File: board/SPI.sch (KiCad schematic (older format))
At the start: 38 parts, among them P14 CONN_5X2, P3 CONN_7X2, U11 MICRO_SD, U17 FXO-HC536R, U26 CB3LV-3I-27M0000, U3 W25Q128FVEIG

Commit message: Importing footprint names into schematic.
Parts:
- C132: footprint (none) -> SM0402
- C188, C189, C241, C244, C36, R116, R117, R118, R119, R16, R17, R18, R19, R20, R21, R40, R41, R60, R61, R62, R63, R64, R76, R80, R81, R82, R83, R86, R93: footprint (none) -> SM0603
- JP1, JP2: footprint (none) -> GS2
- P14: footprint (none) -> PIN_ARRAY_5x2
- P3: footprint (none) -> JTAG
- U11: footprint ~ -> MicroSD
- U17: footprint ~ -> FXO-HC536R
- U26: footprint ~ -> CB3LV-3I
- U3: footprint ~ -> SO8E_N
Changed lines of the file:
@@
 Sheet 4 12
 Title "HDMI2USB"
-Date "5 jul 2015"
+Date "23 jul 2015"
 Rev "Rev2"
 Comp ""
@@
 F 0 "U3" H 3850 6250 60  0000 C CNN
 F 1 "W25Q128FVEIG" H 3850 5400 60  0000 C CNN
-F 2 "~" H 3850 5800 60  0000 C CNN
+F 2 "SO8E_N" H 3850 5800 60  0001 C CNN
 F 3 "~" H 3850 5800 60  0000 C CNN
 F 4 "Yes" H 3850 5800 60  0001 C CNN "Populate"
@@
 F 0 "R16" V 2430 5700 50  0000 C CNN
 F 1 "50R" V 2350 5700 50  0000 C CNN
-F 2 "" H 2350 5700 60  0000 C CNN
+F 2 "SM0603" H 2350 5700 60  0001 C CNN
 F 3 "" H 2350 5700 60  0000 C CNN
 F 4 "Yes" H 2350 5700 60  0001 C CNN "Populate"
@@
 F 0 "R17" V 2430 5850 50  0000 C CNN
 F 1 "50R" V 2350 5850 50  0000 C CNN
-F 2 "" H 2350 5850 60  0000 C CNN
+F 2 "SM0603" H 2350 5850 60  0001 C CNN
 F 3 "" H 2350 5850 60  0000 C CNN
 F 4 "Yes" H 2350 5850 60  0001 C CNN "Populate"
@@
 F 0 "R20" V 3280 5250 50  0000 C CNN
 F 1 "10K" V 3200 5250 50  0000 C CNN
-F 2 "" H 3200 5250 60  0000 C CNN
+F 2 "SM0603" H 3200 5250 60  0001 C CNN
 F 3 "" H 3200 5250 60  0000 C CNN
 F 4 "Yes" H 3200 5250 60  0001 C CNN "Populate"
@@
 F 0 "R19" V 3280 5050 50  0000 C CNN
 F 1 "10K" V 3200 5050 50  0000 C CNN
-F 2 "" H 3200 5050 60  0000 C CNN
+F 2 "SM0603" H 3200 5050 60  0001 C CNN
 F 3 "" H 3200 5050 60  0000 C CNN
 F 4 "Yes" H 3200 5050 60  0001 C CNN "Populate"
@@
 F 0 "R18" V 3280 4850 50  0000 C CNN
 F 1 "10K" V 3200 4850 50  0000 C CNN
-F 2 "" H 3200 4850 60  0000 C CNN
+F 2 "SM0603" H 3200 4850 60  0001 C CNN
 F 3 "" H 3200 4850 60  0000 C CNN
 F 4 "Yes" H 3200 4850 60  0001 C CNN "Populate"
@@
 F 0 "R21" V 5330 5250 50  0000 C CNN
 F 1 "10K" V 5250 5250 50  0000 C CNN
-F 2 "" H 5250 5250 60  0000 C CNN
+F 2 "SM0603" H 5250 5250 60  0001 C CNN
 F 3 "" H 5250 5250 60  0000 C CNN
 F 4 "Yes" H 5250 5250 60  0001 C CNN "Populate"
@@
 F 0 "C36" H 4600 5000 50  0000 L CNN
 F 1 "0.1UF" V 4600 4600 50  0000 L CNN
-F 2 "" H 4550 4900 60  0000 C CNN
+F 2 "SM0603" H 4550 4900 60  0001 C CNN
 F 3 "" H 4550 4900 60  0000 C CNN
 F 4 "Yes" H 4550 4900 60  0001 C CNN "Populate"
@@
 F 0 "JP1" H 5750 1850 60  0000 C CNN
 F 1 "JUMPER" H 5750 1620 40  0000 C CNN
-F 2 "" H 5750 1700 60  0000 C CNN
+F 2 "GS2" H 5750 1700 60  0001 C CNN
 F 3 "" H 5750 1700 60  0000 C CNN
 F 4 "Yes" H 5750 1700 60  0001 C CNN "Populate"
@@
 F 0 "JP2" H 5750 2200 60  0000 C CNN
 F 1 "JUMPER" H 5750 1970 40  0000 C CNN
-F 2 "" H 5750 2050 60  0000 C CNN
+F 2 "GS2" H 5750 2050 60  0001 C CNN
 F 3 "" H 5750 2050 60  0000 C CNN
 F 4 "Yes" H 5750 2050 60  0001 C CNN "Populate"
@@
 F 0 "R60" V 8700 1400 50  0000 C CNN
 F 1 "100K" V 8650 1200 50  0000 C CNN
-F 2 "" H 8650 1200 60  0000 C CNN
+F 2 "SM0603" H 8650 1200 60  0001 C CNN
 F 3 "" H 8650 1200 60  0000 C CNN
 F 4 "Yes" H 8650 1200 60  0001 C CNN "Populate"
@@
 F 0 "R61" V 8700 1550 50  0000 C CNN
 F 1 "100K" V 8650 1350 50  0000 C CNN
-F 2 "" H 8650 1350 60  0000 C CNN
+F 2 "SM0603" H 8650 1350 60  0001 C CNN
 F 3 "" H 8650 1350 60  0000 C CNN
 F 4 "Yes" H 8650 1350 60  0001 C CNN "Populate"
@@
 F 0 "R62" V 8700 1700 50  0000 C CNN
 F 1 "100K" V 8650 1500 50  0000 C CNN
-F 2 "" H 8650 1500 60  0000 C CNN
+F 2 "SM0603" H 8650 1500 60  0001 C CNN
 F 3 "" H 8650 1500 60  0000 C CNN
 F 4 "Yes" H 8650 1500 60  0001 C CNN "Populate"
@@
 F 0 "R63" V 8700 1850 50  0000 C CNN
 F 1 "100K" V 8650 1650 50  0000 C CNN
-F 2 "" H 8650 1650 60  0000 C CNN
+F 2 "SM0603" H 8650 1650 60  0001 C CNN
 F 3 "" H 8650 1650 60  0000 C CNN
 F 4 "Yes" H 8650 1650 60  0001 C CNN "Populate"
@@
 F 0 "R64" V 8750 1700 50  0000 C CNN
 F 1 "100K" V 8650 1800 50  0000 C CNN
-F 2 "" H 8650 1800 60  0000 C CNN
+F 2 "SM0603" H 8650 1800 60  0001 C CNN
 F 3 "" H 8650 1800 60  0000 C CNN
 F 4 "Yes" H 8650 1800 60  0001 C CNN "Populate"
@@
 F 0 "C132" H 8100 1550 50  0000 L CNN
 F 1 "0.1UF" V 7900 1400 50  0000 L CNN
-F 2 "" H 8050 1450 60  0000 C CNN
+F 2 "SM0402" H 8050 1450 60  0001 C CNN
 F 3 "" H 8050 1450 60  0000 C CNN
 F 4 "Yes" H 8050 1450 60  0001 C CNN "Populate"
@@
 F 0 "U17" H 1650 2850 60  0000 C CNN
 F 1 "FXO-HC536R" H 1800 3400 60  0000 C CNN
-F 2 "~" H 1800 3150 60  0000 C CNN
+F 2 "FXO-HC536R" H 1800 3150 60  0001 C CNN
 F 3 "~" H 1800 3150 60  0000 C CNN
 F 4 "Yes" H 1800 3150 60  0001 C CNN "Populate"
@@
 F 0 "R80" V 1550 2900 50  0000 C CNN
 F 1 "4K7" V 1500 2700 50  0000 C CNN
-F 2 "" H 1500 2700 60  0000 C CNN
+F 2 "SM0603" H 1500 2700 60  0001 C CNN
 F 3 "" H 1500 2700 60  0000 C CNN
 F 4 "Yes" H 1500 2700 60  0001 C CNN "Populate"
@@
 F 0 "C188" H 950 3050 50  0000 L CNN
 F 1 "0.1UF" V 750 2900 50  0000 L CNN
-F 2 "" H 900 2950 60  0000 C CNN
+F 2 "SM0603" H 900 2950 60  0001 C CNN
 F 3 "" H 900 2950 60  0000 C CNN
 F 4 "Yes" H 900 2950 60  0001 C CNN "Populate"
@@
 F 0 "C189" H 2450 3650 50  0000 L CNN
 F 1 "15PF" V 2250 3500 50  0000 L CNN
-F 2 "" H 2400 3550 60  0000 C CNN
+F 2 "SM0603" H 2400 3550 60  0001 C CNN
 F 3 "" H 2400 3550 60  0000 C CNN
 F 4 "Yes" H 2400 3550 60  0001 C CNN "Populate"
@@
 F 0 "U11" H 9550 2500 60  0000 C CNN
 F 1 "MICRO_SD" H 9450 2800 60  0000 C CNN
-F 2 "~" H 9550 2350 60  0000 C CNN
+F 2 "MicroSD" H 9550 2350 60  0001 C CNN
 F 3 "~" H 9550 2350 60  0000 C CNN
 F 4 "Yes" H 9550 2350 60  0001 C CNN "Populate"
@@
 F 0 "P3" H 9850 4050 60  0000 C CNN
 F 1 "CONN_7X2" V 9850 4050 60  0001 C CNN
-F 2 "" H 9850 4050 60  0000 C CNN
+F 2 "JTAG" H 9850 4050 60  0001 C CNN
 F 3 "" H 9850 4050 60  0000 C CNN
 F 4 "Yes" H 9850 4050 60  0001 C CNN "Populate"
@@
 F 0 "R40" V 5530 1450 50  0000 C CNN
 F 1 "10K" V 5450 1450 50  0000 C CNN
-F 2 "" H 5450 1450 60  0000 C CNN
+F 2 "SM0603" H 5450 1450 60  0001 C CNN
 F 3 "" H 5450 1450 60  0000 C CNN
 F 4 "Yes" H 5450 1450 60  0001 C CNN "Populate"
@@
 F 0 "R41" V 5530 2300 50  0000 C CNN
 F 1 "10K" V 5450 2300 50  0000 C CNN
-F 2 "" H 5450 2300 60  0000 C CNN
+F 2 "SM0603" H 5450 2300 60  0001 C CNN
 F 3 "" H 5450 2300 60  0000 C CNN
 F 4 "Yes" H 5450 2300 60  0001 C CNN "Populate"
@@
 F 0 "R76" V 9150 3650 50  0000 C CNN
 F 1 "100R" V 9200 3850 50  0000 C CNN
-F 2 "" H 9200 3850 60  0000 C CNN
+F 2 "SM0603" H 9200 3850 60  0001 C CNN
 F 3 "" H 9200 3850 60  0000 C CNN
 F 4 "Yes" H 9200 3850 60  0001 C CNN "Populate"
@@
 F 0 "R81" V 9150 3750 50  0000 C CNN
 F 1 "100R" V 9200 3950 50  0000 C CNN
-F 2 "" H 9200 3950 60  0000 C CNN
+F 2 "SM0603" H 9200 3950 60  0001 C CNN
 F 3 "" H 9200 3950 60  0000 C CNN
 F 4 "Yes" H 9200 3950 60  0001 C CNN "Populate"
@@
 F 0 "R82" V 9150 3850 50  0000 C CNN
 F 1 "100R" V 9200 4050 50  0000 C CNN
-F 2 "" H 9200 4050 60  0000 C CNN
+F 2 "SM0603" H 9200 4050 60  0001 C CNN
 F 3 "" H 9200 4050 60  0000 C CNN
 F 4 "Yes" H 9200 4050 60  0001 C CNN "Populate"
@@
 F 0 "R83" V 9150 3950 50  0000 C CNN
 F 1 "100R" V 9200 4150 50  0000 C CNN
-F 2 "" H 9200 4150 60  0000 C CNN
+F 2 "SM0603" H 9200 4150 60  0001 C CNN
 F 3 "" H 9200 4150 60  0000 C CNN
 F 4 "Yes" H 9200 4150 60  0001 C CNN "Populate"
@@
 F 0 "U26" H 1600 1100 60  0000 C CNN
 F 1 "CB3LV-3I-27M0000" H 1750 1650 60  0000 C CNN
-F 2 "~" H 1750 1400 60  0000 C CNN
+F 2 "CB3LV-3I" H 1750 1400 60  0001 C CNN
 F 3 "~" H 1750 1400 60  0000 C CNN
 F 4 "Yes" H 1750 1400 60  0001 C CNN "Populate"
@@
 F 0 "R86" V 1500 1150 50  0000 C CNN
 F 1 "4K7" V 1450 950 50  0000 C CNN
-F 2 "" H 1450 950 60  0000 C CNN
+F 2 "SM0603" H 1450 950 60  0001 C CNN
 F 3 "" H 1450 950 60  0000 C CNN
 F 4 "Yes" H 1450 950 60  0001 C CNN "Populate"
@@
 F 0 "C241" H 900 1300 50  0000 L CNN
 F 1 "0.1UF" V 700 1150 50  0000 L CNN
-F 2 "" H 850 1200 60  0000 C CNN
+F 2 "SM0603" H 850 1200 60  0001 C CNN
 F 3 "" H 850 1200 60  0000 C CNN
 F 4 "Yes" H 850 1200 60  0001 C CNN "Populate"
@@
 F 0 "C244" H 2400 1900 50  0000 L CNN
 F 1 "15PF" V 2200 1750 50  0000 L CNN
-F 2 "" H 2350 1800 60  0000 C CNN
+F 2 "SM0603" H 2350 1800 60  0001 C CNN
 F 3 "" H 2350 1800 60  0000 C CNN
 F 4 "Yes" H 2350 1800 60  0001 C CNN "Populate"
@@
 F 0 "P14" H 9200 6100 60  0000 C CNN
 F 1 "CONN_5X2" V 9200 5800 50  0001 C CNN
-F 2 "" H 9200 5800 60  0000 C CNN
+F 2 "PIN_ARRAY_5x2" H 9200 5800 60  0001 C CNN
 F 3 "" H 9200 5800 60  0000 C CNN
 F 4 "Yes" H 9200 5800 60  0001 C CNN "Populate"
@@
 F 0 "R93" V 7930 5350 50  0000 C CNN
 F 1 "100R" V 7850 5350 50  0000 C CNN
-F 2 "" H 7850 5350 60  0000 C CNN
+F 2 "SM0603" H 7850 5350 60  0001 C CNN
 F 3 "" H 7850 5350 60  0000 C CNN
 F 4 "Yes" H 7850 5350 60  0001 C CNN "Populate"
@@
 F 0 "R118" V 10030 5600 50  0000 C CNN
 F 1 "100R" V 9950 5600 50  0000 C CNN
-F 2 "" H 9950 5600 60  0000 C CNN
+F 2 "SM0603" H 9950 5600 60  0001 C CNN
 F 3 "" H 9950 5600 60  0000 C CNN
 F 4 "Yes" H 9950 5600 60  0001 C CNN "Populate"
@@
 F 0 "R116" V 8180 5800 50  0000 C CNN
 F 1 "100R" V 8100 5800 50  0000 C CNN
-F 2 "" H 8100 5800 60  0000 C CNN
+F 2 "SM0603" H 8100 5800 60  0001 C CNN
 F 3 "" H 8100 5800 60  0000 C CNN
 F 4 "Yes" H 8100 5800 60  0001 C CNN "Populate"
@@
 F 0 "R117" V 9730 5300 50  0000 C CNN
 F 1 "1M" V 9650 5300 50  0000 C CNN
-F 2 "" H 9650 5300 60  0000 C CNN
+F 2 "SM0603" H 9650 5300 60  0001 C CNN
 F 3 "" H 9650 5300 60  0000 C CNN
 F 4 "Yes" H 9650 5300 60  0001 C CNN "Populate"
@@
 F 0 "R119" V 10000 5650 50  0000 C CNN
 F 1 "1K" V 9950 5900 50  0000 C CNN
-F 2 "" H 9950 5900 60  0000 C CNN
+F 2 "SM0603" H 9950 5900 60  0001 C CNN
 F 3 "" H 9950 5900 60  0000 C CNN
 F 4 "Yes" H 9950 5900 60  0001 C CNN "Populate"

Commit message: Changes on 2015-10-21@7-21PM
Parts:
- added P28: CONN_6, symbol CONN_6
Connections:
- net SD_CLK: now also P28.3
- net SD_CMD: now also P28.4
- net SD_DAT0: now also P28.2
- net SD_DAT1: now also P28.1
- net SD_DAT2: now also P28.6
- net SD_DAT3: now also P28.5
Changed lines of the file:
@@
 Sheet 4 12
 Title "HDMI2USB"
-Date "10 sep 2015"
+Date "19 oct 2015"
 Rev "Rev2"
 Comp ""
@@
 $EndComp
 $Comp
-L GND #PWR023
+L GND #PWR26
 U 1 1 52D67B63
 P 2750 6100
-F 0 "#PWR023" H 2750 6100 30  0001 C CNN
+F 0 "#PWR26" H 2750 6100 30  0001 C CNN
 F 1 "GND" H 2750 6030 30  0001 C CNN
 F 2 "" H 2750 6100 60  0000 C CNN
@@
 $EndComp
 $Comp
-L GND #PWR024
+L GND #PWR27
 U 1 1 52D67F2B
 P 4350 5050
-F 0 "#PWR024" H 4350 5050 30  0001 C CNN
+F 0 "#PWR27" H 4350 5050 30  0001 C CNN
 F 1 "GND" H 4350 4980 30  0001 C CNN
 F 2 "" H 4350 5050 60  0000 C CNN
@@
 FPGA_M1
 $Comp
-L GND #PWR025
+L GND #PWR31
 U 1 1 52E410EA
 P 9850 2850
-F 0 "#PWR025" H 9850 2850 30  0001 C CNN
+F 0 "#PWR31" H 9850 2850 30  0001 C CNN
 F 1 "GND" H 9850 2780 30  0001 C CNN
 F 2 "" H 9850 2850 60  0000 C CNN
@@
 $EndComp
 $Comp
-L GND #PWR026
+L GND #PWR30
 U 1 1 52E4224F
 P 8050 1700
-F 0 "#PWR026" H 8050 1700 30  0001 C CNN
+F 0 "#PWR30" H 8050 1700 30  0001 C CNN
 F 1 "GND" H 8050 1630 30  0001 C CNN
 F 2 "" H 8050 1700 60  0000 C CNN
@@
 	1    0    0    -1
 $EndComp
-Text HLabel 8000 2600 0    60   BiDi ~ 12
+Text HLabel 7950 2550 2    60   BiDi ~ 12
 SD_DAT0
-Text HLabel 8000 2700 0    60   BiDi ~ 12
+Text HLabel 7500 2650 2    60   BiDi ~ 12
 SD_DAT1
-Text HLabel 8000 2400 0    60   Input ~ 12
+Text HLabel 8000 2350 2    60   Input ~ 12
 SD_CLK
-Text HLabel 8000 2200 0    60   BiDi ~ 12
+Text HLabel 7400 2200 2    60   BiDi ~ 12
 SD_CMD
-Text HLabel 8000 2100 0    60   BiDi ~ 12
+Text HLabel 7400 2100 2    60   BiDi ~ 12
 SD_DAT3
-Text HLabel 8000 2000 0    60   BiDi ~ 12
+Text HLabel 7400 2000 2    60   BiDi ~ 12
 SD_DAT2
 Text Label 7800 1200 0    60   ~ 0
@@
 JTAG\n
 $Comp
-L GND #PWR027
+L GND #PWR32
 U 1 1 52E36A0E
 P 10350 4450
-F 0 "#PWR027" H 10350 4450 30  0001 C CNN
+F 0 "#PWR32" H 10350 4450 30  0001 C CNN
 F 1 "GND" H 10350 4380 30  0001 C CNN
 F 2 "" H 10350 4450 60  0000 C CNN
@@
 $EndComp
 $Comp
-L GND #PWR028
+L GND #PWR23
 U 1 1 52E638C7
 P 900 3400
-F 0 "#PWR028" H 900 3400 30  0001 C CNN
+F 0 "#PWR23" H 900 3400 30  0001 C CNN
 F 1 "GND" H 900 3330 30  0001 C CNN
 F 2 "" H 900 3400 60  0000 C CNN
@@
 $EndComp
 $Comp
-L GND #PWR029
+L GND #PWR25
 U 1 1 530C0275
 P 2400 3850
-F 0 "#PWR029" H 2400 3850 30  0001 C CNN
+F 0 "#PWR25" H 2400 3850 30  0001 C CNN
 F 1 "GND" H 2400 3780 30  0001 C CNN
 F 2 "" H 2400 3850 60  0000 C CNN
@@
 VCC3V3
 $Comp
-L GND #PWR030
+L GND #PWR28
 U 1 1 5392B9BD
 P 6650 2000
-F 0 "#PWR030" H 6650 2000 30  0001 C CNN
+F 0 "#PWR28" H 6650 2000 30  0001 C CNN
 F 1 "GND" H 6650 1930 30  0001 C CNN
 F 2 "" H 6650 2000 60  0000 C CNN
@@
 Connection ~ 9850 2800
 Wire Wire Line
-	8000 2600 9250 2600
-Wire Wire Line
-	8000 2700 9250 2700
+	7950 2600 9250 2600
+Wire Wire Line
+	7500 2700 9250 2700
 Wire Wire Line
 	8000 2400 9250 2400
@@
 	8950 1650 8950 2600
 Wire Wire Line
-	8000 2200 9250 2200
+	7400 2200 9250 2200
 Wire Wire Line
 	9000 2200 9000 1500
@@
 	9000 1500 8900 1500
 Wire Wire Line
-	8000 2100 9250 2100
+	7400 2100 9250 2100
 Wire Wire Line
 	9050 2100 9050 1350
@@
 	9100 1200 9100 2000
 Wire Wire Line
-	8000 2000 9250 2000
+	7400 2000 9250 2000
 Connection ~ 8950 2600
 Connection ~ 8900 2700
@@
 $EndComp
 $Comp
-L GND #PWR031
+L GND #PWR22
 U 1 1 551C2E78
 P 850 1650
-F 0 "#PWR031" H 850 1650 30  0001 C CNN
+F 0 "#PWR22" H 850 1650 30  0001 C CNN
 F 1 "GND" H 850 1580 30  0001 C CNN
 F 2 "" H 850 1650 60  0000 C CNN
@@
 $EndComp
 $Comp
-L GND #PWR032
+L GND #PWR24
 U 1 1 551C2E86
 P 2350 2100
-F 0 "#PWR032" H 2350 2100 30  0001 C CNN
+F 0 "#PWR24" H 2350 2100 30  0001 C CNN
 F 1 "GND" H 2350 2030 30  0001 C CNN
 F 2 "" H 2350 2100 60  0000 C CNN
@@
 	7850 5800 7750 5800
 $Comp
-L GND #PWR033
+L GND #PWR33
 U 1 1 551DEA2A
 P 10400 5950
-F 0 "#PWR033" H 10400 5950 30  0001 C CNN
+F 0 "#PWR33" H 10400 5950 30  0001 C CNN
 F 1 "GND" H 10400 5880 30  0001 C CNN
 F 2 "" H 10400 5950 60  0000 C CNN
@@
 NoConn ~ 8800 6000
 $Comp
-L GND #PWR034
+L GND #PWR29
 U 1 1 551DEF69
 P 7750 5900
-F 0 "#PWR034" H 7750 5900 30  0001 C CNN
+F 0 "#PWR29" H 7750 5900 30  0001 C CNN
 F 1 "GND" H 7750 5830 30  0001 C CNN
 F 2 "" H 7750 5900 60  0000 C CNN
@@
 Text Label 9650 4950 0    60   ~ 0
 VCC1V5
+$Comp
+L CONN_6 P28
+U 1 1 56254665
+P 7050 2250
+F 0 "P28" V 7000 2250 60  0000 C CNN
+F 1 "CONN_6" V 7100 2250 60  0000 C CNN
+F 2 "" H 7050 2250 60  0000 C CNN
+F 3 "" H 7050 2250 60  0000 C CNN
+	1    7050 2250
+	-1   0    0    1
+$EndComp
+Wire Wire Line
+	8000 2400 8000 2300
+Wire Wire Line
+	8000 2300 7400 2300
+Wire Wire Line
+	7400 2400 7950 2400
+Wire Wire Line
+	7500 2700 7500 2500
+Wire Wire Line
+	7500 2500 7400 2500
+Wire Wire Line
+	7950 2400 7950 2600
 $EndSCHEMATC

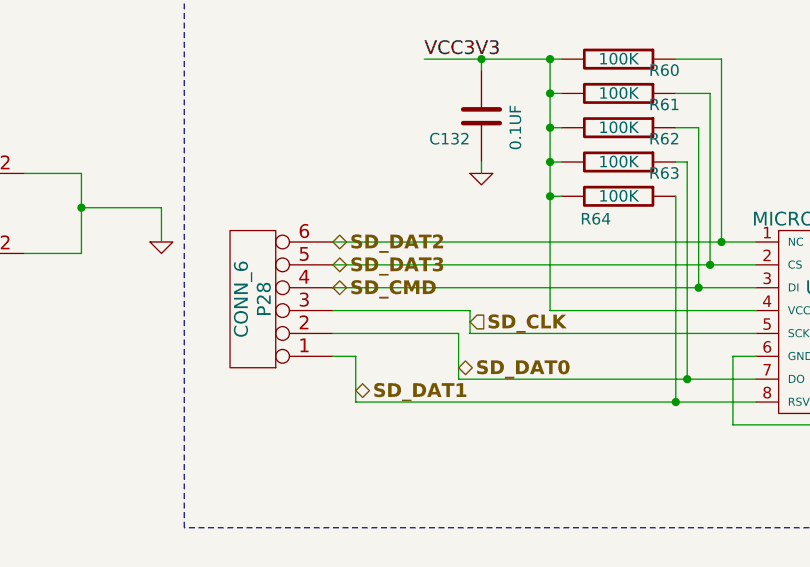
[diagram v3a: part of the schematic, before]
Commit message: Changes on 12-11-2015 Micro SD header added.#35
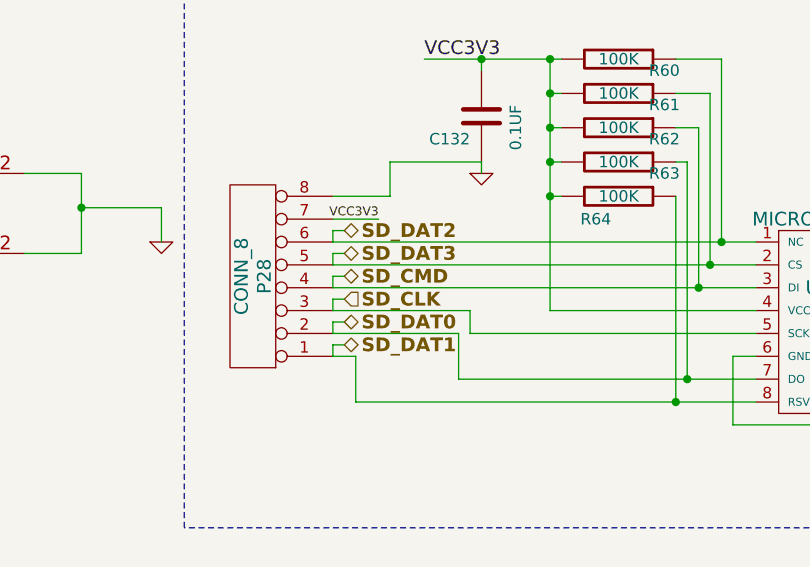
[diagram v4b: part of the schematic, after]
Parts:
- removed P28: CONN_6, symbol CONN_6
- added P28: CONN_8, symbol CONN_8
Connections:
- net GND: now also P28.8 (P8)
- net SD_CLK: now also P28.3 (P3)
- net SD_CMD: now also P28.4 (P4)
- net SD_DAT0: now also P28.2 (P2)
- net SD_DAT1: now also P28.1 (P1)
- net SD_DAT2: now also P28.6 (P6)
- net SD_DAT3: now also P28.5 (P5)
- net VCC3V3: now also P28.7 (P7)

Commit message: Final changes
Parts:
- C132, C188, C241, C36: value 0.1UF -> 0.1uF
- C189, C244: value 15PF -> 15pF
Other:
- note added: "135MHz"
- note removed: "100MHz"
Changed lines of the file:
@@
 LIBS:contrib
 LIBS:valves
-LIBS:hdmi2usb
-LIBS:timvideos-pcie-8x
 LIBS:HDMI2USB-cache
 EELAYER 27 0
@@
 Sheet 4 12
 Title "HDMI2USB"
-Date "2 nov 2015"
+Date "9 nov 2015"
 Rev "Rev2"
 Comp ""
@@
 $EndComp
 $Comp
-L GND #PWR26
+L GND #PWR023
 U 1 1 52D67B63
 P 2750 6100
-F 0 "#PWR26" H 2750 6100 30  0001 C CNN
+F 0 "#PWR023" H 2750 6100 30  0001 C CNN
 F 1 "GND" H 2750 6030 30  0001 C CNN
 F 2 "" H 2750 6100 60  0000 C CNN
@@
 P 4550 4900
 F 0 "C36" H 4600 5000 50  0000 L CNN
-F 1 "0.1UF" V 4600 4600 50  0000 L CNN
+F 1 "0.1uF" V 4600 4600 50  0000 L CNN
 F 2 "SM0603" H 4550 4900 60  0001 C CNN
 F 3 "" H 4550 4900 60  0000 C CNN
@@
 $EndComp
 $Comp
-L GND #PWR27
+L GND #PWR024
 U 1 1 52D67F2B
 P 4350 5050
-F 0 "#PWR27" H 4350 5050 30  0001 C CNN
+F 0 "#PWR024" H 4350 5050 30  0001 C CNN
 F 1 "GND" H 4350 4980 30  0001 C CNN
 F 2 "" H 4350 5050 60  0000 C CNN
@@
 FPGA_M1
 $Comp
-L GND #PWR31
+L GND #PWR025
 U 1 1 52E410EA
 P 9850 2850
-F 0 "#PWR31" H 9850 2850 30  0001 C CNN
+F 0 "#PWR025" H 9850 2850 30  0001 C CNN
 F 1 "GND" H 9850 2780 30  0001 C CNN
 F 2 "" H 9850 2850 60  0000 C CNN
@@
 P 8050 1450
 F 0 "C132" H 8100 1550 50  0000 L CNN
-F 1 "0.1UF" V 7900 1400 50  0000 L CNN
+F 1 "0.1uF" V 7900 1400 50  0000 L CNN
 F 2 "SM0402" H 8050 1450 60  0001 C CNN
 F 3 "" H 8050 1450 60  0000 C CNN
@@
 $EndComp
 $Comp
-L GND #PWR30
+L GND #PWR026
 U 1 1 52E4224F
 P 8050 1700
-F 0 "#PWR30" H 8050 1700 30  0001 C CNN
+F 0 "#PWR026" H 8050 1700 30  0001 C CNN
 F 1 "GND" H 8050 1630 30  0001 C CNN
 F 2 "" H 8050 1700 60  0000 C CNN
@@
 JTAG\n
 $Comp
-L GND #PWR32
+L GND #PWR027
 U 1 1 52E36A0E
 P 10350 4450
-F 0 "#PWR32" H 10350 4450 30  0001 C CNN
+F 0 "#PWR027" H 10350 4450 30  0001 C CNN
 F 1 "GND" H 10350 4380 30  0001 C CNN
 F 2 "" H 10350 4450 60  0000 C CNN
@@
 P 900 2950
 F 0 "C188" H 950 3050 50  0000 L CNN
-F 1 "0.1UF" V 750 2900 50  0000 L CNN
+F 1 "0.1uF" V 750 2900 50  0000 L CNN
 F 2 "SM0603" H 900 2950 60  0001 C CNN
 F 3 "" H 900 2950 60  0000 C CNN
@@
 $EndComp
 $Comp
-L GND #PWR23
+L GND #PWR028
 U 1 1 52E638C7
 P 900 3400
-F 0 "#PWR23" H 900 3400 30  0001 C CNN
+F 0 "#PWR028" H 900 3400 30  0001 C CNN
 F 1 "GND" H 900 3330 30  0001 C CNN
 F 2 "" H 900 3400 60  0000 C CNN
@@
 P 2400 3550
 F 0 "C189" H 2450 3650 50  0000 L CNN
-F 1 "15PF" V 2250 3500 50  0000 L CNN
+F 1 "15pF" V 2250 3500 50  0000 L CNN
 F 2 "SM0603" H 2400 3550 60  0001 C CNN
 F 3 "" H 2400 3550 60  0000 C CNN
@@
 $EndComp
 $Comp
-L GND #PWR25
+L GND #PWR029
 U 1 1 530C0275
 P 2400 3850
-F 0 "#PWR25" H 2400 3850 30  0001 C CNN
+F 0 "#PWR029" H 2400 3850 30  0001 C CNN
 F 1 "GND" H 2400 3780 30  0001 C CNN
 F 2 "" H 2400 3850 60  0000 C CNN
@@
 VCC3V3
 $Comp
-L GND #PWR28
+L GND #PWR030
 U 1 1 5392B9BD
 P 6650 2000
-F 0 "#PWR28" H 6650 2000 30  0001 C CNN
+F 0 "#PWR030" H 6650 2000 30  0001 C CNN
 F 1 "GND" H 6650 1930 30  0001 C CNN
 F 2 "" H 6650 2000 60  0000 C CNN
@@
 $EndComp
 Text Notes 2550 3200 0    60   ~ 0
-100MHz
+135MHz
 $Comp
 L FXO-HC536R U26
@@
 P 850 1200
 F 0 "C241" H 900 1300 50  0000 L CNN
-F 1 "0.1UF" V 700 1150 50  0000 L CNN
+F 1 "0.1uF" V 700 1150 50  0000 L CNN
 F 2 "SM0603" H 850 1200 60  0001 C CNN
 F 3 "" H 850 1200 60  0000 C CNN
@@
 $EndComp
 $Comp
-L GND #PWR22
+L GND #PWR031
 U 1 1 551C2E78
 P 850 1650
-F 0 "#PWR22" H 850 1650 30  0001 C CNN
+F 0 "#PWR031" H 850 1650 30  0001 C CNN
 F 1 "GND" H 850 1580 30  0001 C CNN
 F 2 "" H 850 1650 60  0000 C CNN
@@
 P 2350 1800
 F 0 "C244" H 2400 1900 50  0000 L CNN
-F 1 "15PF" V 2200 1750 50  0000 L CNN
+F 1 "15pF" V 2200 1750 50  0000 L CNN
 F 2 "SM0603" H 2350 1800 60  0001 C CNN
 F 3 "" H 2350 1800 60  0000 C CNN
@@
 $EndComp
 $Comp
-L GND #PWR24
+L GND #PWR032
 U 1 1 551C2E86
 P 2350 2100
-F 0 "#PWR24" H 2350 2100 30  0001 C CNN
+F 0 "#PWR032" H 2350 2100 30  0001 C CNN
 F 1 "GND" H 2350 2030 30  0001 C CNN
 F 2 "" H 2350 2100 60  0000 C CNN
@@
 $EndComp
 $Comp
-L GND #PWR33
+L GND #PWR033
 U 1 1 551DEA2A
 P 10400 5950
-F 0 "#PWR33" H 10400 5950 30  0001 C CNN
+F 0 "#PWR033" H 10400 5950 30  0001 C CNN
 F 1 "GND" H 10400 5880 30  0001 C CNN
 F 2 "" H 10400 5950 60  0000 C CNN
@@
 NoConn ~ 8800 6000
 $Comp
-L GND #PWR29
+L GND #PWR034
 U 1 1 551DEF69
 P 7750 5900
-F 0 "#PWR29" H 7750 5900 30  0001 C CNN
+F 0 "#PWR034" H 7750 5900 30  0001 C CNN
 F 1 "GND" H 7750 5830 30  0001 C CNN
 F 2 "" H 7750 5900 60  0000 C CNN
